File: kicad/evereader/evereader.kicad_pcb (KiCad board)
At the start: 2 copper layers, 186 x 132 mm, 74 parts, among them J1 USB-C-2.0-RECEPTACLE, J2 MICRO-SD-CARD-READER, J5 JST_SH_01x02_1.0mm, J6 JST_SH_02x04_1.0mm, J7 JST_SH_02x04_1.0mm, J8 JST_SH_01x02_1.0mm, Q1 FS8205A, SW1 SW_Push, SW2 SW_Push, SW3 SW_Push, SW4 2_PIN_SW, SW5 2_PIN_SW, U1 TP4056-42-ESOP8, U2 DW01A, U3 AP2112K-3.3, U5 ESP32-S3-WROOM-1-N16-R8

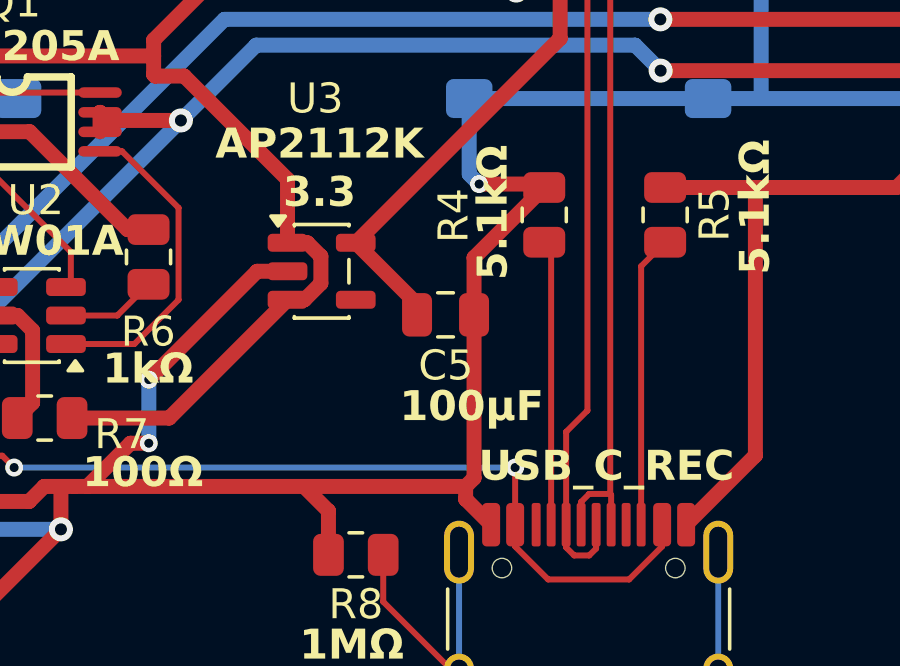
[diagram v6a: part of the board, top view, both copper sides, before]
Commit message: actually swapped the footprint of C5 from 0805 to 1026
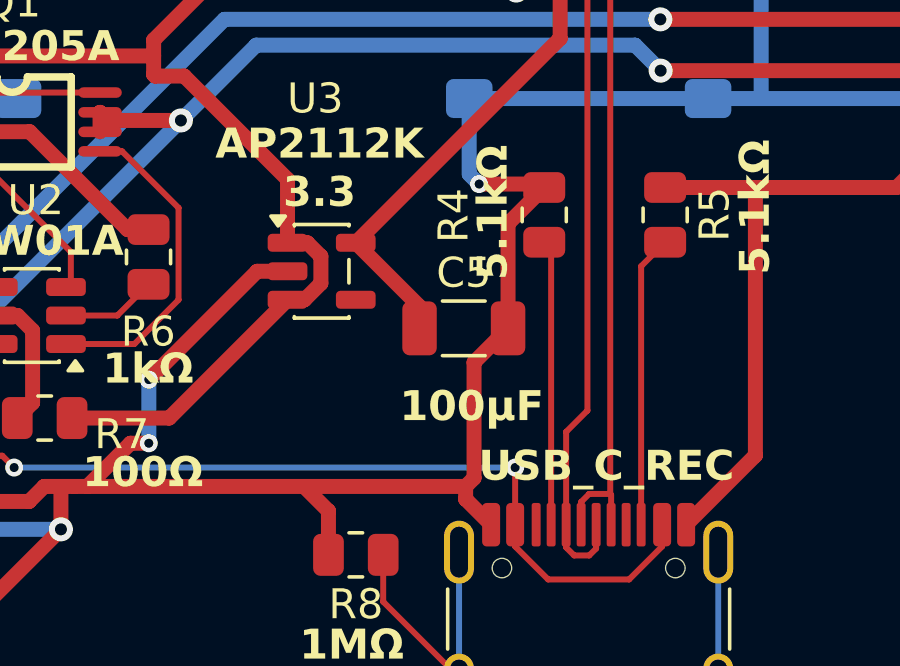
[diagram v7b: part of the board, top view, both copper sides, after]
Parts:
- C5: footprint Capacitor_SMD:C_0805_2012Metric -> Capacitor_SMD:C_1206_3216Metric
- moved C5 0.76 mm to (77.0, 144.9)
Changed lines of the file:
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@@
 		)
 	)
-	(footprint "Capacitor_SMD:C_0805_2012Metric"
+	(footprint "Capacitor_SMD:C_1206_3216Metric"
 		(layer "F.Cu")
-		(at 76.391471 144.48)
-		(descr "Capacitor SMD 0805 (2012 Metric), square (rectangular) end terminal, IPC-7351 nominal, (Body size source: IPC-SM-782 page 76, https://www.pcb-3d.com/wordpress/wp-content/uploads/ipc-sm-782a_amendment_1_and_2.pdf, https://docs.google.com/spreadsheets/d/1BsfQQcO9C6DZCsRaXUlFlo91Tg2WpOkGARC1WS5S8t0/edit?usp=sharing)")
+		(at 77 144.93)
+		(descr "Capacitor SMD 1206 (3216 Metric), square (rectangular) end terminal, IPC-7351 nominal, (Body size source: IPC-SM-782 page 76, https://www.pcb-3d.com/wordpress/wp-content/uploads/ipc-sm-782a_amendment_1_and_2.pdf)")
 		(tags "capacitor")
 		(property "Reference" "C5"
-			(at 0.008529 1.69 0)
+			(at 0 -1.85 0)
 			(layer "F.SilkS")
 			(effects
@@
 		)
 		(property "Value" "100μF"
-			(at 0 1.68 0)
+			(at 0 1.85 0)
 			(layer "F.Fab")
 			(effects
@@
 		(duplicate_pad_numbers_are_jumpers no)
 		(fp_line
-			(start -0.261252 -0.735)
-			(end 0.261252 -0.735)
+			(start -0.711252 -0.91)
+			(end 0.711252 -0.91)
 			(stroke
 				(width 0.12)
@@
 		)
 		(fp_line
-			(start -0.261252 0.735)
-			(end 0.261252 0.735)
+			(start -0.711252 0.91)
+			(end 0.711252 0.91)
 			(stroke
 				(width 0.12)
@@
 		)
 		(fp_rect
-			(start -1.7 -0.98)
-			(end 1.7 0.98)
+			(start -2.3 -1.15)
+			(end 2.3 1.15)
 			(stroke
 				(width 0.05)
@@
 		)
 		(fp_rect
-			(start -1 -0.625)
-			(end 1 0.625)
+			(start -1.6 -0.8)
+			(end 1.6 0.8)
 			(stroke
 				(width 0.1)
@@
 			(effects
 				(font
-					(size 0.5 0.5)
-					(thickness 0.08)
+					(size 0.8 0.8)
+					(thickness 0.12)
 				)
 			)
 		)
 		(pad "1" smd roundrect
-			(at -0.95 0)
-			(size 1 1.45)
+			(at -1.475 0)
+			(size 1.15 1.8)
 			(layers "F.Cu" "F.Mask" "F.Paste")
-			(roundrect_rratio 0.25)
+			(roundrect_rratio 0.217391)
 			(net "+3.3V")
 			(pintype "passive")
 		)
 		(pad "2" smd roundrect
-			(at 0.95 0)
-			(size 1 1.45)
+			(at 1.475 0)
+			(size 1.15 1.8)
 			(layers "F.Cu" "F.Mask" "F.Paste")
-			(roundrect_rratio 0.25)
+			(roundrect_rratio 0.217391)
 			(net "GND")
 			(pintype "passive")
 		)
 		(embedded_fonts no)
-		(model "${KICAD10_3DMODEL_DIR}/Capacitor_SMD.3dshapes/C_0805_2012Metric.step"
+		(model "${KICAD10_3DMODEL_DIR}/Capacitor_SMD.3dshapes/C_1206_3216Metric.step"
 			(offset
 				(xyz 0 0 0)
@@
 	)
 	(segment
+		(start 78.475 144.93)
+		(end 77.341471 146.063529)
+		(width 0.5)
+		(layer "F.Cu")
+		(net "GND")
+	)
+	(segment
 		(start 55.586471 142.935)
 		(end 55.921471 143.27)
@@
 	)
 	(segment
-		(start 77.341471 144.48)
-		(end 77.341471 142.575)
-		(width 0.5)
-		(layer "F.Cu")
-		(net "GND")
-	)
-	(segment
 		(start 79.611471 36.787918)
 		(end 89.866627 36.787918)
@@
 	)
 	(segment
+		(start 78.475 141.441471)
+		(end 78.475 144.93)
+		(width 0.5)
+		(layer "F.Cu")
+		(net "GND")
+	)
+	(segment
 		(start 99.181471 57.6)
 		(end 99.211471 57.57)
@@
 	)
 	(segment
+		(start 79.681471 140.235)
+		(end 78.475 141.441471)
+		(width 0.5)
+		(layer "F.Cu")
+		(net "GND")
+	)
+	(segment
 		(start 58.411471 44.67)
 		(end 58.411471 43.82)
@@
 	)
 	(segment
-		(start 77.341471 142.575)
-		(end 79.681471 140.235)
-		(width 0.5)
-		(layer "F.Cu")
-		(net "GND")
-	)
-	(segment
 		(start 73.436471 75.995)
 		(end 75.986471 75.995)
@@
 	)
 	(segment
+		(start 77.341471 146.063529)
+		(end 77.341471 149.92)
+		(width 0.5)
+		(layer "F.Cu")
+		(net "GND")
+	)
+	(segment
 		(start 120.525 86.445)
 		(end 120.525 98.88)
@@
 	)
 	(segment
-		(start 77.341471 144.48)
-		(end 77.341471 149.92)
-		(width 0.5)
-		(layer "F.Cu")
-		(net "GND")
-	)
-	(segment
 		(start 72.261471 77.17)
 		(end 73.436471 75.995)
@@
 	)
 	(segment
-		(start 73.398971 142.0775)
-		(end 75.441471 144.12)
-		(width 0.5)
-		(layer "F.Cu")
-		(net "+3.3V")
-	)
-	(segment
 		(start 76.236471 81.475)
 		(end 78.936471 78.775)
@@
 	)
 	(segment
+		(start 73.398971 142.0775)
+		(end 75.525 144.203529)
+		(width 0.5)
+		(layer "F.Cu")
+		(net "+3.3V")
+	)
+	(segment
 		(start 69.253971 85.3275)
 		(end 69.861471 85.935)
@@
 	)
 	(segment
-		(start 75.441471 144.12)
-		(end 75.441471 144.48)
-		(width 0.5)
-		(layer "F.Cu")
-		(net "+3.3V")
-	)
-	(segment
 		(start 70.361471 77.17)
 		(end 68.261471 79.27)
@@
 		(width 0.5)
 		(layer "F.Cu")
+		(net "+3.3V")
+	)
+	(segment
+		(start 75.525 144.203529)
+		(end 75.525 144.93)
+		(width 0.5)
+		(layer "F.Cu")
